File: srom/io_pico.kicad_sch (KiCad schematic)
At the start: 7 parts, among them J201 Conn_01x03_Female, J202 Conn_01x06_Female, U201 Pico-2 IO, U202 APS6404L-3SQR_PSRAM64Mbit

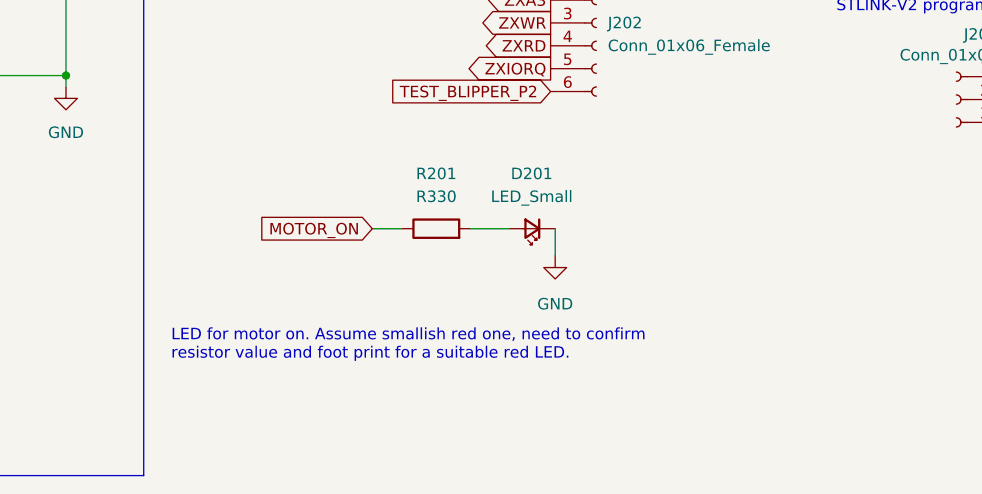
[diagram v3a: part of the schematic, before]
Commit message: add 2 switches as buttons for the UI
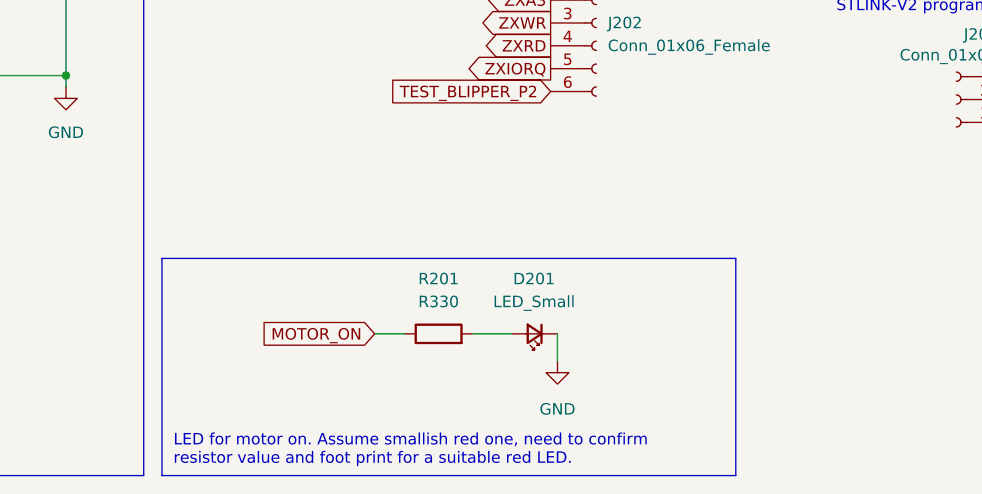
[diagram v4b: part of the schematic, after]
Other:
- moved on the sheet: D201, R201
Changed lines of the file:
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@@
   (no_connect (at 186.182 40.132))
   (no_connect (at 92.202 56.388))
-  (wire (pts (xy 166.37 124.206) (xy 170.688 124.206))
+  (polyline (pts (xy 195.834 127.508) (xy 132.08 127.508))
+    (stroke (width 0) (type default) (color 0 0 0 0))
+  )
+  (wire (pts (xy 166.624 135.89) (xy 170.942 135.89))
     (stroke (width 0) (type default) (color 0 0 0 0))
   )
@@
     (stroke (width 0) (type default) (color 0 0 0 0))
   )
-  (wire (pts (xy 175.768 127.254) (xy 175.768 124.206))
+  (wire (pts (xy 176.022 138.938) (xy 176.022 135.89))
     (stroke (width 0) (type default) (color 0 0 0 0))
   )
@@
     (stroke (width 0) (type default) (color 0 0 0 0))
   )
+  (polyline (pts (xy 195.834 151.638) (xy 195.834 127.508))
+    (stroke (width 0) (type default) (color 0 0 0 0))
+  )
   (wire (pts (xy 74.422 84.328) (xy 74.422 95.758))
     (stroke (width 0) (type default) (color 0 0 0 0))
@@
     (stroke (width 0) (type default) (color 0 0 0 0))
   )
+  (polyline (pts (xy 132.08 151.638) (xy 195.834 151.638))
+    (stroke (width 0) (type default) (color 0 0 0 0))
+  )
   (wire (pts (xy 26.67 74.168) (xy 26.67 107.188))
     (stroke (width 0) (type default) (color 0 0 0 0))
@@
     (stroke (width 0) (type default) (color 0 0 0 0))
   )
+  (polyline (pts (xy 132.08 127.508) (xy 132.08 151.638))
+    (stroke (width 0) (type default) (color 0 0 0 0))
+  )
   (wire (pts (xy 100.838 41.148) (xy 106.172 41.148))
     (stroke (width 0) (type default) (color 0 0 0 0))
   )
-  (wire (pts (xy 155.448 124.206) (xy 158.75 124.206))
+  (wire (pts (xy 155.702 135.89) (xy 159.004 135.89))
     (stroke (width 0) (type default) (color 0 0 0 0))
   )
@@
   )
   (text "LED for motor on. Assume smallish red one, need to confirm\nresistor value and foot print for a suitable red LED."
-    (at 133.096 138.938 0)
+    (at 133.35 150.622 0)
     (effects (font (size 1.27 1.27)) (justify left bottom))
   )
@@
     )
   )
-  (global_label "MOTOR_ON" (shape input) (at 155.448 124.206 180) (fields_autoplaced)
-    (effects (font (size 1.27 1.27)) (justify right))
-    (property "Intersheet References" "${INTERSHEET_REFS}" (id 0) (at 143.0563 124.1266 0)
+  (global_label "MOTOR_ON" (shape input) (at 155.702 135.89 180) (fields_autoplaced)
+    (effects (font (size 1.27 1.27)) (justify right))
+    (property "Intersheet References" "${INTERSHEET_REFS}" (id 0) (at 143.3103 135.8106 0)
       (effects (font (size 1.27 1.27)) (justify right) hide)
     )
@@
     )
   )
-  (symbol (lib_id "power:GND") (at 175.768 127.254 0) (unit 1)
+  (symbol (lib_id "power:GND") (at 176.022 138.938 0) (unit 1)
     (in_bom yes) (on_board yes) (fields_autoplaced)
-    (property "Reference" "#PWR0106" (id 0) (at 175.768 133.604 0)
-      (effects (font (size 1.27 1.27)) hide)
-    )
-    (property "Value" "GND" (id 1) (at 175.768 132.588 0))
-    (property "Footprint" "" (id 2) (at 175.768 127.254 0)
-      (effects (font (size 1.27 1.27)) hide)
-    )
-    (property "Datasheet" "" (id 3) (at 175.768 127.254 0)
+    (property "Reference" "#PWR0106" (id 0) (at 176.022 145.288 0)
+      (effects (font (size 1.27 1.27)) hide)
+    )
+    (property "Value" "GND" (id 1) (at 176.022 144.272 0))
+    (property "Footprint" "" (id 2) (at 176.022 138.938 0)
+      (effects (font (size 1.27 1.27)) hide)
+    )
+    (property "Datasheet" "" (id 3) (at 176.022 138.938 0)
       (effects (font (size 1.27 1.27)) hide)
     )
@@
     (pin "1")
   )
-  (symbol (lib_id "Device:LED_Small") (at 173.228 124.206 180) (unit 1)
+  (symbol (lib_id "Device:LED_Small") (at 173.482 135.89 180) (unit 1)
     (in_bom yes) (on_board yes) (fields_autoplaced)
-    (property "Reference" "D201" (id 0) (at 173.1645 118.11 0))
-    (property "Value" "LED_Small" (id 1) (at 173.1645 120.65 0))
-    (property "Footprint" "LED_THT:LED_D3.0mm" (id 2) (at 173.228 124.206 90)
-      (effects (font (size 1.27 1.27)) hide)
-    )
-    (property "Datasheet" "~" (id 3) (at 173.228 124.206 90)
+    (property "Reference" "D201" (id 0) (at 173.4185 129.794 0))
+    (property "Value" "LED_Small" (id 1) (at 173.4185 132.334 0))
+    (property "Footprint" "LED_THT:LED_D3.0mm" (id 2) (at 173.482 135.89 90)
+      (effects (font (size 1.27 1.27)) hide)
+    )
+    (property "Datasheet" "~" (id 3) (at 173.482 135.89 90)
       (effects (font (size 1.27 1.27)) hide)
     )
@@
     (pin "1")
   )
-  (symbol (lib_id "Device:R") (at 162.56 124.206 90) (unit 1)
+  (symbol (lib_id "Device:R") (at 162.814 135.89 90) (unit 1)
     (in_bom yes) (on_board yes) (fields_autoplaced)
-    (property "Reference" "R201" (id 0) (at 162.56 118.11 90))
-    (property "Value" "R330" (id 1) (at 162.56 120.65 90))
-    (property "Footprint" "Resistor_SMD:R_1206_3216Metric_Pad1.30x1.75mm_HandSolder" (id 2) (at 162.56 125.984 90)
-      (effects (font (size 1.27 1.27)) hide)
-    )
-    (property "Datasheet" "~" (id 3) (at 162.56 124.206 0)
-      (effects (font (size 1.27 1.27)) hide)
-    )
+    (property "Reference" "R201" (id 0) (at 162.814 129.794 90))
+    (property "Value" "R330" (id 1) (at 162.814 132.334 90))
+    (property "Footprint" "Resistor_SMD:R_1206_3216Metric_Pad1.30x1.75mm_HandSolder" (id 2) (at 162.814 137.668 90)
+      (effects (font (size 1.27 1.27)) hide)
+    )
+    (property "Datasheet" "~" (id 3) (at 162.814 135.89 0)
+      (effects (font (size 1.27 1.27)) hide)
+    )

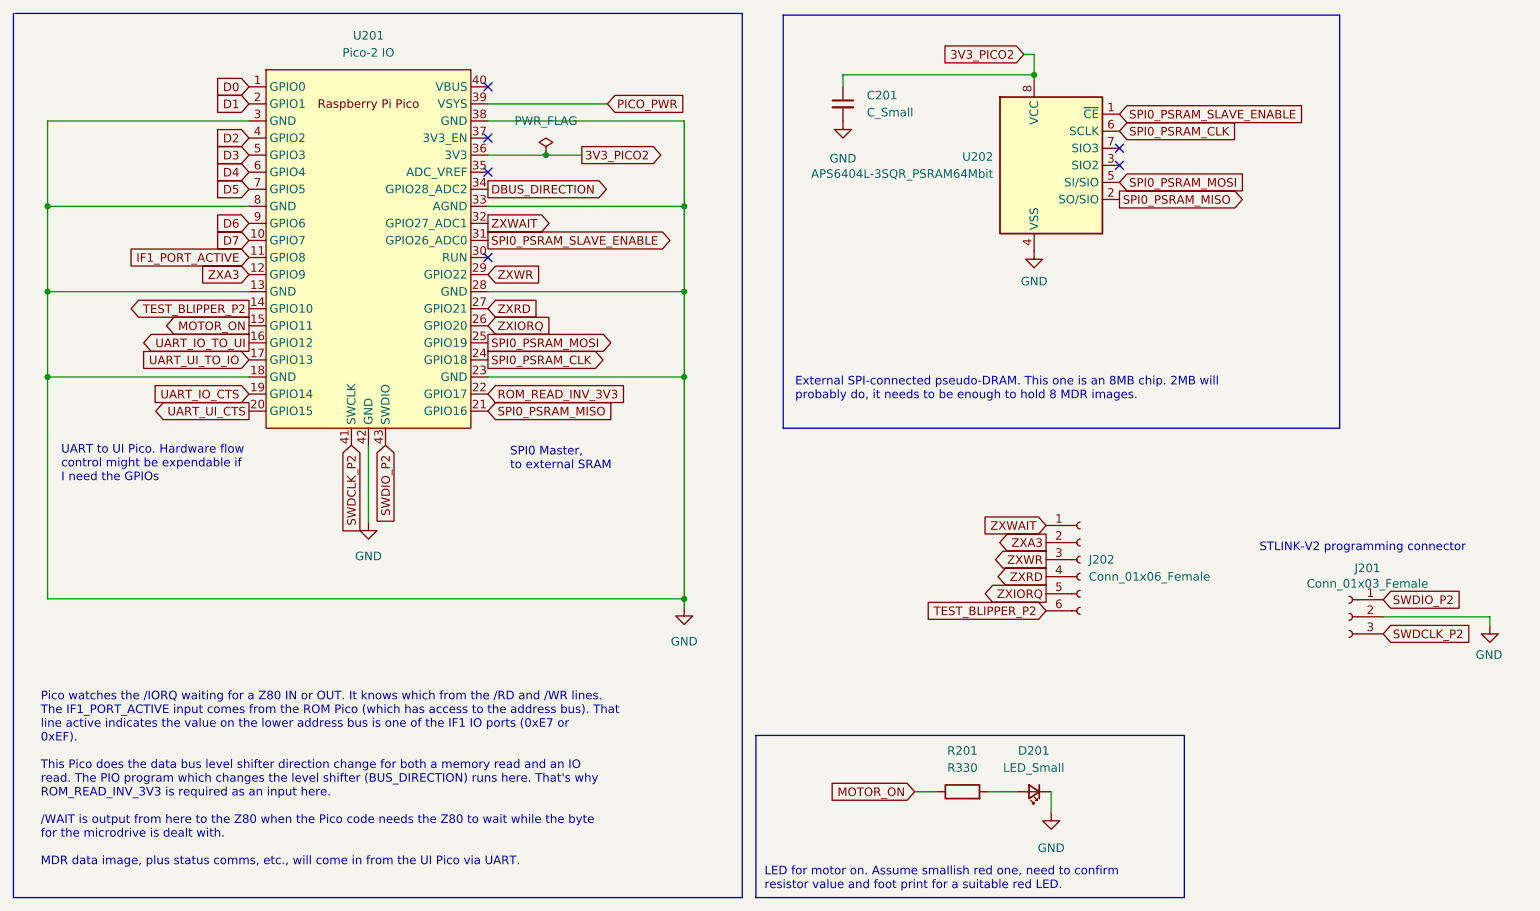
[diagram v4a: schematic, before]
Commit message: update schematic, remove uart UI/IO link, replace with PIO link
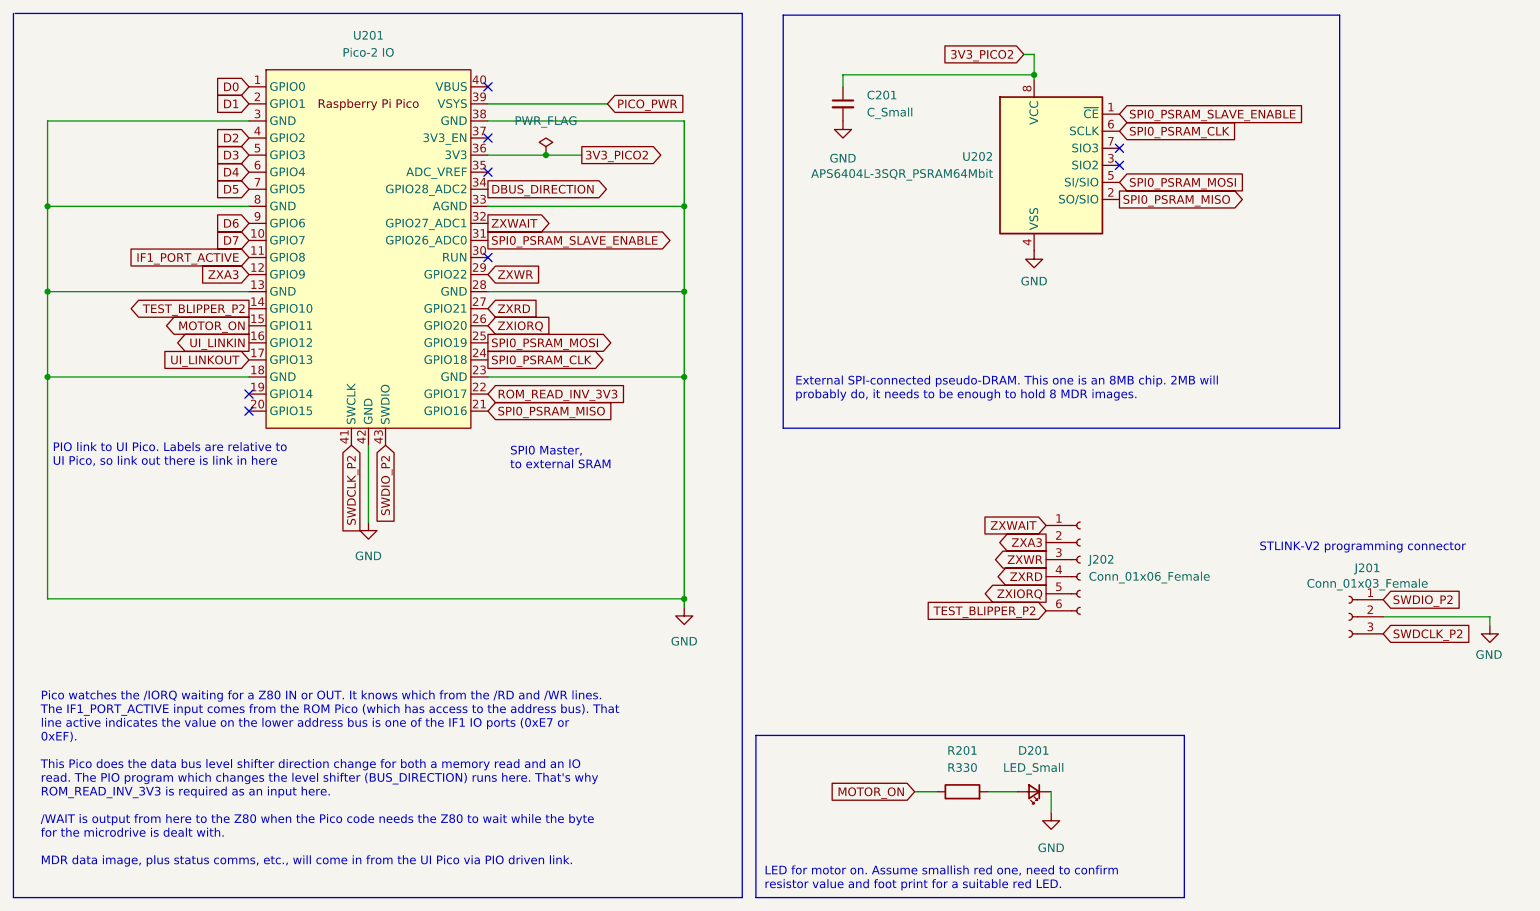
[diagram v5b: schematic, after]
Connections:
- net UART_IO_CTS: no longer names the net of U201.19 (GPIO14)
- net UART_IO_TO_UI renamed UI_LINKIN
- net UART_UI_CTS: no longer names the net of U201.20 (GPIO15)
- net UART_UI_TO_IO renamed UI_LINKOUT
- no-connect marks 6 -> 8
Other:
- note added: "PIO link to UI Pico. Labels are relative to UI Pico, so link out there is link in here"
- note removed: "UART to UI Pico. Hardware flow control might be expendable if I need the GPIOs"
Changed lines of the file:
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@@
   (no_connect (at 92.202 30.988))
   (no_connect (at 92.202 43.688))
+  (no_connect (at 56.642 76.708))
   (no_connect (at 186.182 42.672))
   (no_connect (at 92.202 38.608))
   (no_connect (at 186.182 40.132))
   (no_connect (at 92.202 56.388))
+  (no_connect (at 56.642 79.248))
   (polyline (pts (xy 195.834 127.508) (xy 132.08 127.508))
     (stroke (width 0) (type default) (color 0 0 0 0))
@@
     (effects (font (size 1.27 1.27)) (justify left bottom))
   )
-  (text "Pico watches the /IORQ waiting for a Z80 IN or OUT. It knows which from the /RD and /WR lines.\nThe IF1_PORT_ACTIVE input comes from the ROM Pico (which has access to the address bus). That\nline active indicates the value on the lower address bus is one of the IF1 IO ports (0xE7 or\n0xEF).\n\nThis Pico does the data bus level shifter direction change for both a memory read and an IO\nread. The PIO program which changes the level shifter (BUS_DIRECTION) runs here. That's why\nROM_READ_INV_3V3 is required as an input here.\n\n/WAIT is output from here to the Z80 when the Pico code needs the Z80 to wait while the byte\nfor the microdrive is dealt with.\n\nMDR data image, plus status comms, etc., will come in from the UI Pico via UART.\n"
+  (text "Pico watches the /IORQ waiting for a Z80 IN or OUT. It knows which from the /RD and /WR lines.\nThe IF1_PORT_ACTIVE input comes from the ROM Pico (which has access to the address bus). That\nline active indicates the value on the lower address bus is one of the IF1 IO ports (0xE7 or\n0xEF).\n\nThis Pico does the data bus level shifter direction change for both a memory read and an IO\nread. The PIO program which changes the level shifter (BUS_DIRECTION) runs here. That's why\nROM_READ_INV_3V3 is required as an input here.\n\n/WAIT is output from here to the Z80 when the Pico code needs the Z80 to wait while the byte\nfor the microdrive is dealt with.\n\nMDR data image, plus status comms, etc., will come in from the UI Pico via PIO driven link.\n"
     (at 25.654 147.066 0)
     (effects (font (size 1.27 1.27)) (justify left bottom))
@@
     (effects (font (size 1.27 1.27)) (justify left bottom))
   )
-  (text "UART to UI Pico. Hardware flow\ncontrol might be expendable if\nI need the GPIOs"
-    (at 28.702 89.916 0)
+  (text "PIO link to UI Pico. Labels are relative to\nUI Pico, so link out there is link in here"
+    (at 27.432 87.63 0)
     (effects (font (size 1.27 1.27)) (justify left bottom))
   )
@@
     )
   )
-  (global_label "UART_IO_CTS" (shape input) (at 56.642 76.708 180) (fields_autoplaced)
-    (effects (font (size 1.27 1.27)) (justify right))
-    (property "Intersheet References" "${INTERSHEET_REFS}" (id 0) (at 42.2546 76.6286 0)
-      (effects (font (size 1.27 1.27)) (justify right) hide)
-    )
-  )
   (global_label "SPI0_PSRAM_CLK" (shape output) (at 92.202 71.628 0) (fields_autoplaced)
     (effects (font (size 1.27 1.27)) (justify left))
@@
     )
   )
-  (global_label "UART_UI_TO_IO" (shape input) (at 56.642 71.628 180) (fields_autoplaced)
-    (effects (font (size 1.27 1.27)) (justify right))
-    (property "Intersheet References" "${INTERSHEET_REFS}" (id 0) (at 40.5008 71.5486 0)
+  (global_label "UI_LINKOUT" (shape input) (at 56.642 71.628 180) (fields_autoplaced)
+    (effects (font (size 1.27 1.27)) (justify right))
+    (property "Intersheet References" "${INTERSHEET_REFS}" (id 0) (at 43.4641 71.5486 0)
       (effects (font (size 1.27 1.27)) (justify right) hide)
     )
@@
     )
   )
-  (global_label "UART_IO_TO_UI" (shape output) (at 56.642 69.088 180) (fields_autoplaced)
-    (effects (font (size 1.27 1.27)) (justify right))
-    (property "Intersheet References" "${INTERSHEET_REFS}" (id 0) (at 40.5008 69.0086 0)
+  (global_label "UI_LINKIN" (shape output) (at 56.642 69.088 180) (fields_autoplaced)
+    (effects (font (size 1.27 1.27)) (justify right))
+    (property "Intersheet References" "${INTERSHEET_REFS}" (id 0) (at 45.1575 69.0086 0)
       (effects (font (size 1.27 1.27)) (justify right) hide)
     )
@@
     )
   )
-  (global_label "UART_UI_CTS" (shape output) (at 56.642 79.248 180) (fields_autoplaced)
-    (effects (font (size 1.27 1.27)) (justify right))
-    (property "Intersheet References" "${INTERSHEET_REFS}" (id 0) (at 42.2546 79.1686 0)
-      (effects (font (size 1.27 1.27)) (justify right) hide)
-    )
-  )
